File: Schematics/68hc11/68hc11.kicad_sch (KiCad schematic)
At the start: 50 parts, among them J1 USB3076-30-A, J2 DB9_Female, J3 Conn_01x10_Male, J4 Conn_01x10_Male, J5 Conn_01x10_Male, J6 Conn_01x10_Male, J7 Conn_01x10_Male, SW1 Reset, U1 MC68HC11A1CC-PLLC, U10 MCP100-270D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

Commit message: Another attempted layout
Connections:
- net GND: now also J1.SH (Shield); no longer J1.6 (Shield)
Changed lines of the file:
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@@
       (effects (font (size 1.27 1.27)) hide)
     )
+    (pin "1")
+    (pin "2")
+    (pin "3")
+    (pin "4")
+    (pin "5")
+    (pin "6")
+    (pin "10")
+    (pin "8")
+    (pin "9")
     (pin "11")
     (pin "12")
     (pin "13")
+    (pin "14")
+    (pin "7")
   )
   (symbol (lib_id "power:VCC") (at 132.08 132.08 0) (unit 1)
@@
     (pin "2")
     (pin "3")
+    (pin "4")
+    (pin "5")
+    (pin "6")
+    (pin "10")
+    (pin "8")
+    (pin "9")
+    (pin "11")
+    (pin "12")
+    (pin "13")
+    (pin "14")
+    (pin "7")
   )
   (symbol (lib_id "Device:C_Polarized_US") (at 215.9 156.21 270) (unit 1)
@@
       (effects (font (size 1.27 1.27)) hide)
     )
+    (pin "1")
+    (pin "2")
+    (pin "3")
+    (pin "4")
+    (pin "5")
+    (pin "6")
+    (pin "10")
+    (pin "8")
+    (pin "9")
+    (pin "11")
+    (pin "12")
+    (pin "13")
     (pin "14")
     (pin "7")
@@
       (effects (font (size 1.27 1.27)) hide)
     )
+    (pin "1")
+    (pin "2")
+    (pin "4")
+    (pin "5")
+    (pin "6")
+    (pin "10")
+    (pin "12")
+    (pin "13")
+    (pin "8")
+    (pin "9")
     (pin "14")
     (pin "7")
@@
     (pin "1")
     (pin "2")
+    (pin "3")
+    (pin "4")
+    (pin "5")
+    (pin "6")
+    (pin "8")
+    (pin "9")
+    (pin "10")
+    (pin "11")
+    (pin "12")
+    (pin "13")
+    (pin "14")
+    (pin "7")
   )
   (symbol (lib_id "Device:C_Polarized_US") (at 218.44 91.44 270) (unit 1)
@@
       (effects (font (size 1.27 1.27)) hide)
     )
-    (pin "10")
-    (pin "8")
-    (pin "9")
+    (pin "1")
+    (pin "2")
+    (pin "3")
+    (pin "4")
+    (pin "5")
+    (pin "6")
+    (pin "10")
+    (pin "8")
+    (pin "9")
+    (pin "11")
+    (pin "12")
+    (pin "13")
+    (pin "14")
+    (pin "7")
   )
   (symbol (lib_id "power:VCC") (at 48.514 72.39 0) (unit 1)
@@
       (effects (font (size 1.27 1.27)) hide)
     )
+    (pin "1")
+    (pin "2")
+    (pin "3")
+    (pin "4")
+    (pin "5")
+    (pin "6")
+    (pin "10")
+    (pin "8")
+    (pin "9")
+    (pin "11")
+    (pin "12")
+    (pin "13")
     (pin "14")
     (pin "7")
@@
     (pin "5")
     (pin "6")
+    (pin "10")
+    (pin "12")
+    (pin "13")
+    (pin "8")
+    (pin "9")
+    (pin "14")
+    (pin "7")
   )
   (symbol (lib_id "power:GND") (at 381 127 0) (unit 1)
@@
       (effects (font (size 1.27 1.27)) hide)
     )
-    (pin "4")
-    (pin "5")
-    (pin "6")
+    (pin "1")
+    (pin "2")
+    (pin "3")
+    (pin "4")
+    (pin "5")
+    (pin "6")
+    (pin "10")
+    (pin "8")
+    (pin "9")
+    (pin "11")
+    (pin "12")
+    (pin "13")
+    (pin "14")
+    (pin "7")
   )
   (symbol (lib_id "power:GND") (at 180.34 52.07 0) (unit 1)
@@
       (effects (font (size 1.27 1.27)) hide)
     )
+    (pin "1")
+    (pin "2")
+    (pin "3")
+    (pin "4")
+    (pin "5")
+    (pin "6")
+    (pin "8")
+    (pin "9")
+    (pin "10")
+    (pin "11")
+    (pin "12")
+    (pin "13")
     (pin "14")
     (pin "7")
@@
     (pin "4")
     (pin "5")
-    (pin "6")
+    (pin "SH")
   )
   (symbol (lib_id "Device:C_Polarized_US") (at 384.81 127 270) (unit 1)
@@
     (pin "2")
     (pin "3")
+    (pin "4")
+    (pin "5")
+    (pin "6")
+    (pin "10")
+    (pin "8")
+    (pin "9")
+    (pin "11")
+    (pin "12")
+    (pin "13")
+    (pin "14")
+    (pin "7")
   )
   (symbol (lib_id "power:VCC") (at 375.92 154.94 0) (unit 1)

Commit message: Still working on it
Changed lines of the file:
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@@
     (stroke (width 0) (type default) (color 0 0 0 0))
   )
-  (wire (pts (xy 166.878 60.198) (xy 168.91 60.198))
-    (stroke (width 0) (type default) (color 0 0 0 0))
-  )
   (wire (pts (xy 313.69 199.39) (xy 321.31 199.39))
     (stroke (width 0) (type default) (color 0 0 0 0))
@@
     (stroke (width 0) (type default) (color 0 0 0 0))
   )
-  (wire (pts (xy 119.38 62.23) (xy 189.23 62.23))
+  (wire (pts (xy 119.38 62.23) (xy 125.73 62.23))
     (stroke (width 0) (type default) (color 0 0 0 0))
   )
@@
     (stroke (width 0) (type default) (color 0 0 0 0))
   )
-  (wire (pts (xy 189.23 59.817) (xy 168.91 59.817))
-    (stroke (width 0) (type default) (color 0 0 0 0))
-  )
   (bus (pts (xy 242.57 236.22) (xy 242.57 238.76))
     (stroke (width 0) (type default) (color 0 0 0 0))
@@
     (stroke (width 0) (type default) (color 0 0 0 0))
   )
-  (wire (pts (xy 168.91 60.198) (xy 168.91 59.817))
-    (stroke (width 0) (type default) (color 0 0 0 0))
-  )
   (bus (pts (xy 200.66 173.99) (xy 200.66 176.53))
     (stroke (width 0) (type default) (color 0 0 0 0))
@@
     (stroke (width 0) (type default) (color 0 0 0 0))
   )
-  (wire (pts (xy 166.878 59.69) (xy 166.878 60.198))
-    (stroke (width 0) (type default) (color 0 0 0 0))
-  )
   (wire (pts (xy 59.69 55.88) (xy 78.74 55.88))
     (stroke (width 0) (type default) (color 0 0 0 0))
@@
       (effects (font (size 1.27 1.27)) hide)
     )
-    (pin "1")
-    (pin "2")
-    (pin "3")
-    (pin "4")
-    (pin "5")
-    (pin "6")
-    (pin "10")
-    (pin "8")
-    (pin "9")
     (pin "11")
     (pin "12")
     (pin "13")
-    (pin "14")
-    (pin "7")
   )
   (symbol (lib_id "power:VCC") (at 132.08 132.08 0) (unit 1)
@@
     (pin "2")
     (pin "3")
-    (pin "4")
-    (pin "5")
-    (pin "6")
-    (pin "10")
-    (pin "8")
-    (pin "9")
-    (pin "11")
-    (pin "12")
-    (pin "13")
-    (pin "14")
-    (pin "7")
   )
   (symbol (lib_id "Device:C_Polarized_US") (at 215.9 156.21 270) (unit 1)
@@
       (effects (font (size 1.27 1.27)) hide)
     )
-    (pin "1")
-    (pin "2")
-    (pin "3")
-    (pin "4")
-    (pin "5")
-    (pin "6")
-    (pin "10")
-    (pin "8")
-    (pin "9")
-    (pin "11")
-    (pin "12")
-    (pin "13")
     (pin "14")
     (pin "7")
@@
       (effects (font (size 1.27 1.27)) hide)
     )
-    (pin "1")
-    (pin "2")
-    (pin "4")
-    (pin "5")
-    (pin "6")
-    (pin "10")
-    (pin "12")
-    (pin "13")
-    (pin "8")
-    (pin "9")
     (pin "14")
     (pin "7")
@@
     (pin "1")
     (pin "2")
-    (pin "3")
-    (pin "4")
-    (pin "5")
-    (pin "6")
-    (pin "8")
-    (pin "9")
-    (pin "10")
-    (pin "11")
-    (pin "12")
-    (pin "13")
-    (pin "14")
-    (pin "7")
   )
   (symbol (lib_id "Device:C_Polarized_US") (at 218.44 91.44 270) (unit 1)
@@
       (effects (font (size 1.27 1.27)) hide)
     )
-    (pin "1")
-    (pin "2")
-    (pin "3")
-    (pin "4")
-    (pin "5")
-    (pin "6")
     (pin "10")
     (pin "8")
     (pin "9")
-    (pin "11")
-    (pin "12")
-    (pin "13")
-    (pin "14")
-    (pin "7")
   )
   (symbol (lib_id "power:VCC") (at 48.514 72.39 0) (unit 1)
@@
       (effects (font (size 1.27 1.27)) hide)
     )
-    (pin "1")
-    (pin "2")
-    (pin "3")
-    (pin "4")
-    (pin "5")
-    (pin "6")
-    (pin "10")
-    (pin "8")
-    (pin "9")
-    (pin "11")
-    (pin "12")
-    (pin "13")
     (pin "14")
     (pin "7")
@@
     (pin "5")
     (pin "6")
-    (pin "10")
-    (pin "12")
-    (pin "13")
-    (pin "8")
-    (pin "9")
-    (pin "14")
-    (pin "7")
   )
   (symbol (lib_id "power:GND") (at 381 127 0) (unit 1)
@@
       (effects (font (size 1.27 1.27)) hide)
     )
-    (pin "1")
-    (pin "2")
-    (pin "3")
     (pin "4")
     (pin "5")
     (pin "6")
-    (pin "10")
-    (pin "8")
-    (pin "9")
-    (pin "11")
-    (pin "12")
-    (pin "13")
-    (pin "14")
-    (pin "7")
   )
   (symbol (lib_id "power:GND") (at 180.34 52.07 0) (unit 1)
@@
       (effects (font (size 1.27 1.27)) hide)
     )
-    (pin "1")
-    (pin "2")
-    (pin "3")
-    (pin "4")
-    (pin "5")
-    (pin "6")
-    (pin "8")
-    (pin "9")
-    (pin "10")
-    (pin "11")
-    (pin "12")
-    (pin "13")
     (pin "14")
     (pin "7")
@@
     (pin "2")
     (pin "3")
-    (pin "4")
-    (pin "5")
-    (pin "6")
-    (pin "10")
-    (pin "8")
-    (pin "9")
-    (pin "11")
-    (pin "12")
-    (pin "13")
-    (pin "14")
-    (pin "7")
   )
   (symbol (lib_id "power:VCC") (at 375.92 154.94 0) (unit 1)

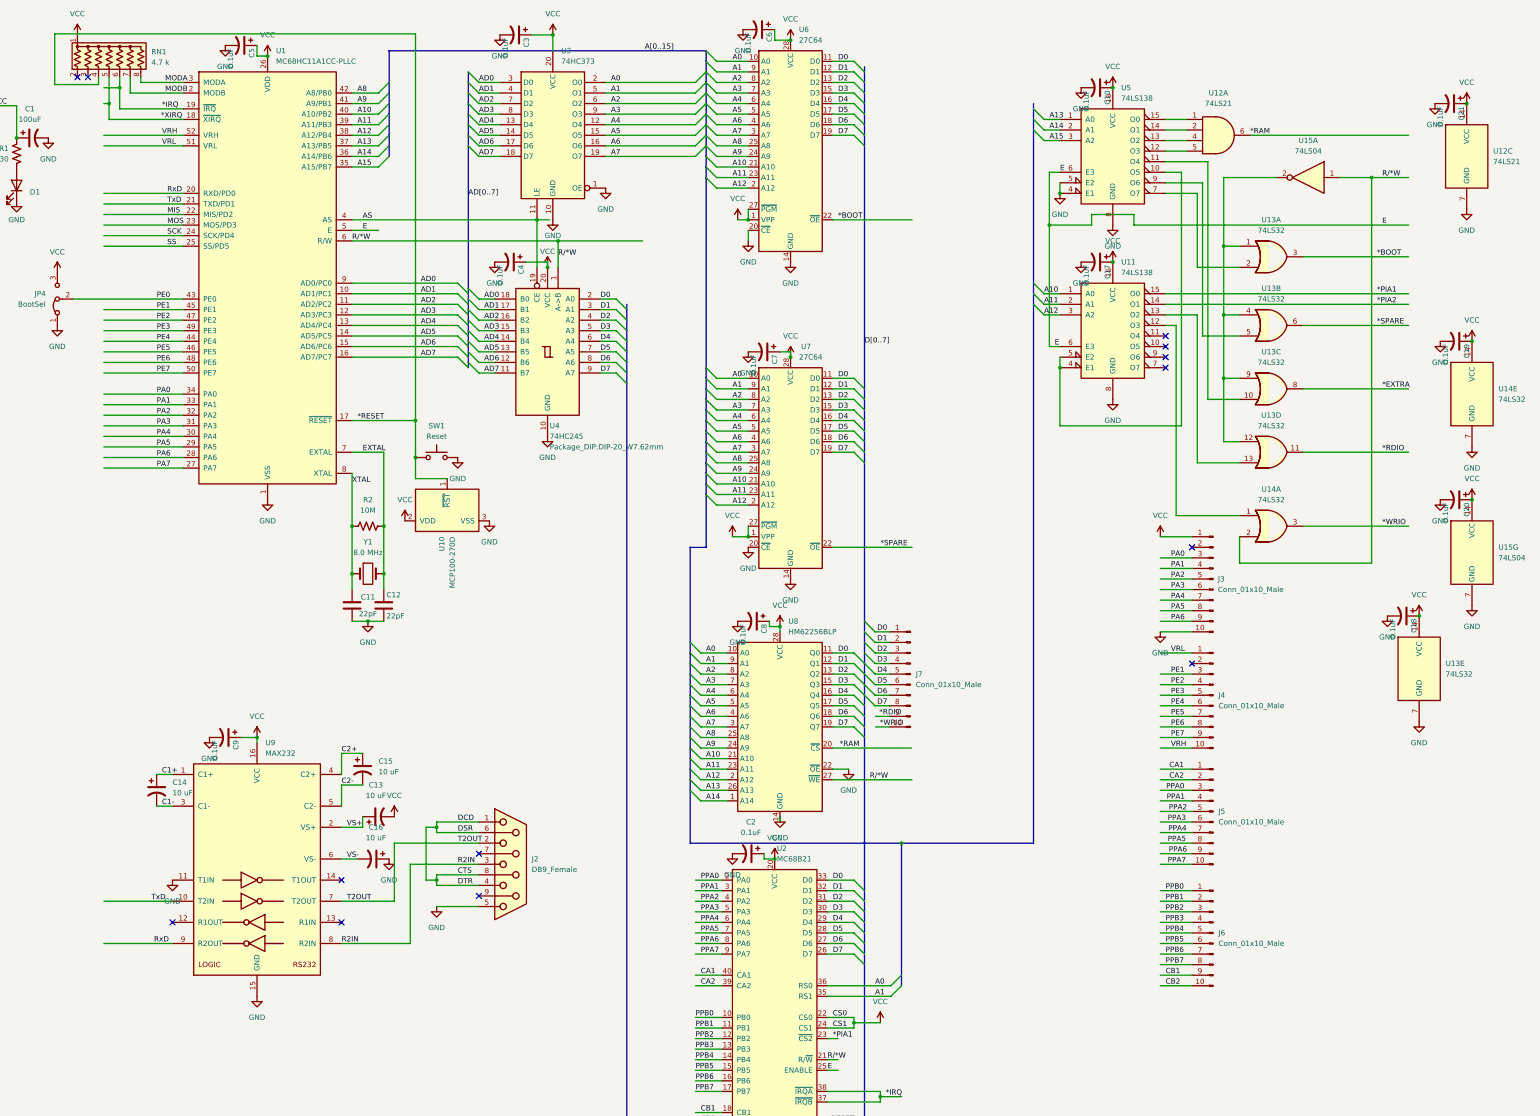
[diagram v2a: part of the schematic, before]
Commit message: Added the Extra ROM Scocket
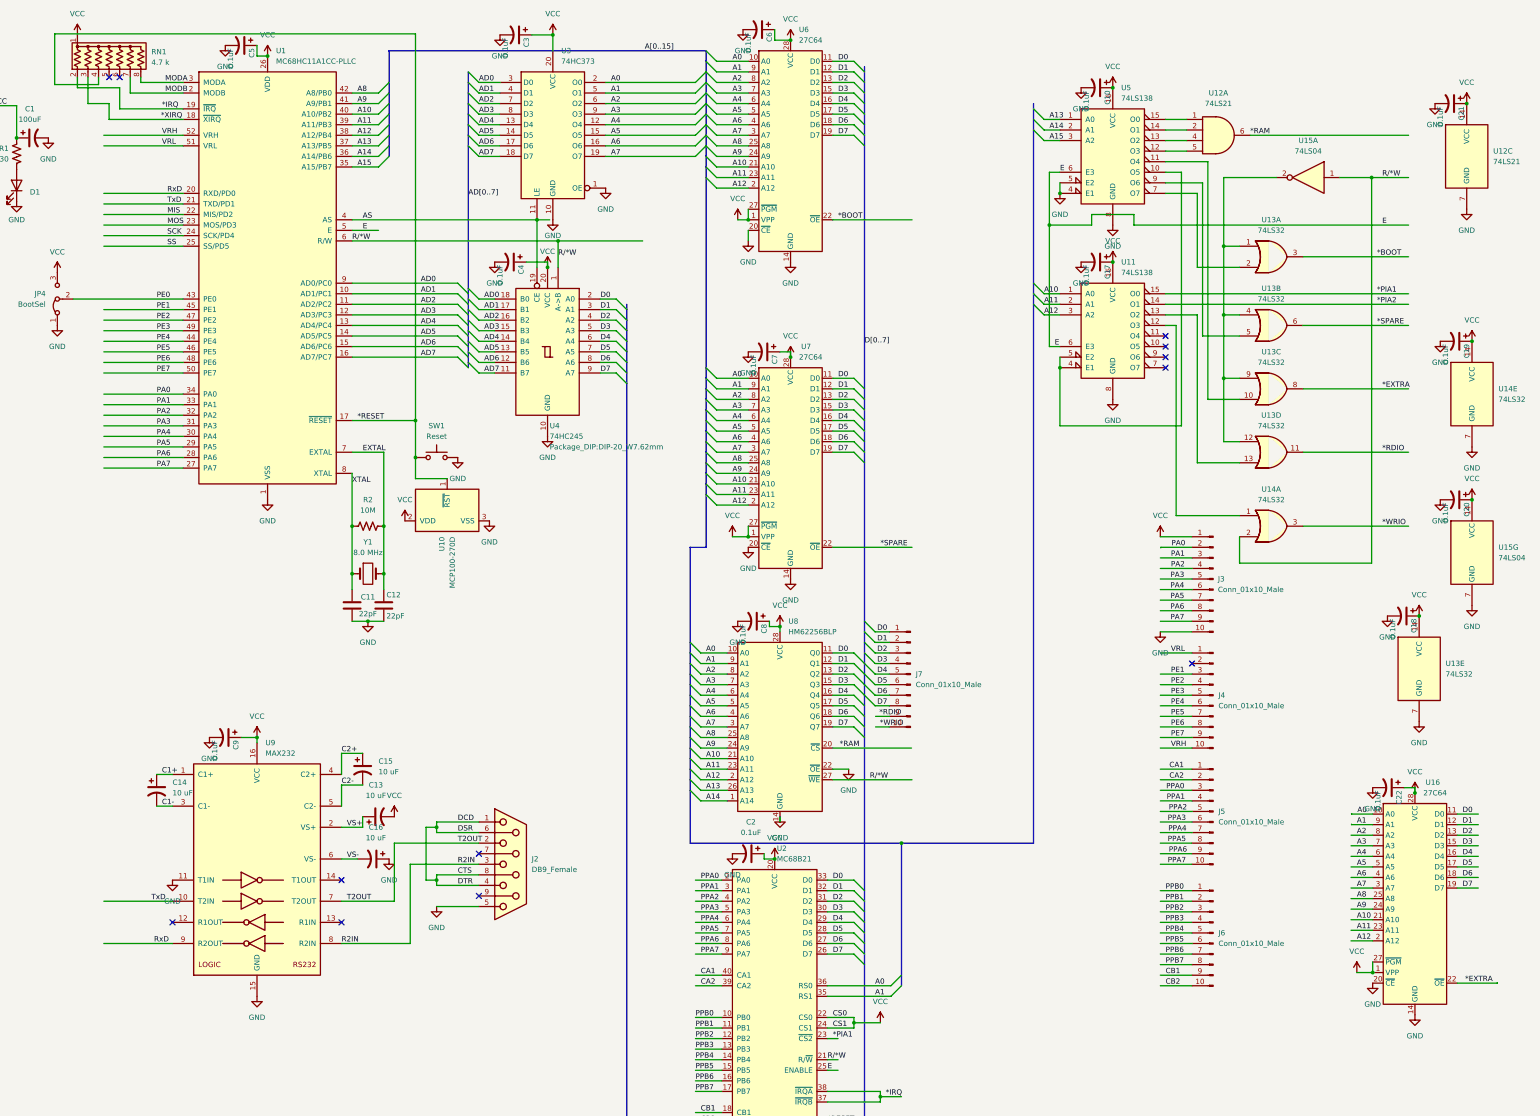
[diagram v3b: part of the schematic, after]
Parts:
- added C22: 0.1uF, Capacitor_THT:C_Disc_D3.0mm_W2.0mm_P2.50mm, symbol Device:C_Polarized_US
- added U16: 27C64, Package_DIP:DIP-28_W15.24mm, symbol Memory_EPROM:27C64
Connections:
- net *EXTRA: now also U16.22 (~{OE})
- net *IRQ: now also RN1.2 (R1); no longer RN1.6 (R5)
- net *XIRQ: now also RN1.3 (R2); no longer RN1.5 (R4)
- net A0: now also U16.10 (A0)
- net A1: now also U16.9 (A1)
- net A10: now also U16.21 (A10)
- net A11: now also U16.23 (A11)
- net A12: now also U16.2 (A12)
- net A2: now also U16.8 (A2)
- net A3: now also U16.7 (A3)
- net A4: now also U16.6 (A4)
- net A5: now also U16.5 (A5)
- net A6: now also U16.4 (A6)
- net A7: now also U16.3 (A7)
- net A8: now also U16.25 (A8)
- net A9: now also U16.24 (A9)
- net D0: now also U16.11 (D0)
- net D1: now also U16.12 (D1)
- net D2: now also U16.13 (D2)
- net D3: now also U16.15 (D3)
- net D4: now also U16.16 (D4)
- net D5: now also U16.17 (D5)
- net D6: now also U16.18 (D6)
- net D7: now also U16.19 (D7)
- net GND: now also C22.2, U16.14 (GND), U16.20 (~{CE})
- net PA0: now also J3.2 (Pin_2); no longer J3.3 (Pin_3)
- net PA1: now also J3.3 (Pin_3); no longer J3.4 (Pin_4)
- net PA2: now also J3.4 (Pin_4); no longer J3.5 (Pin_5)
- net PA3: now also J3.5 (Pin_5); no longer J3.6 (Pin_6)
- net PA4: now also J3.6 (Pin_6); no longer J3.7 (Pin_7)
- net PA5: now also J3.7 (Pin_7); no longer J3.8 (Pin_8)
- net PA6: now also J3.8 (Pin_8); no longer J3.9 (Pin_9)
- net PA7: now also J3.9 (Pin_9)
- net VCC: now also C22.1, U16.1 (VPP), U16.27 (~{PGM}), U16.28 (VCC)
- no-connect marks 16 -> 15
